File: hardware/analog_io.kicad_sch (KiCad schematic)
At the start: 32 parts, among them U1 TLV9162, U2 OPA1678

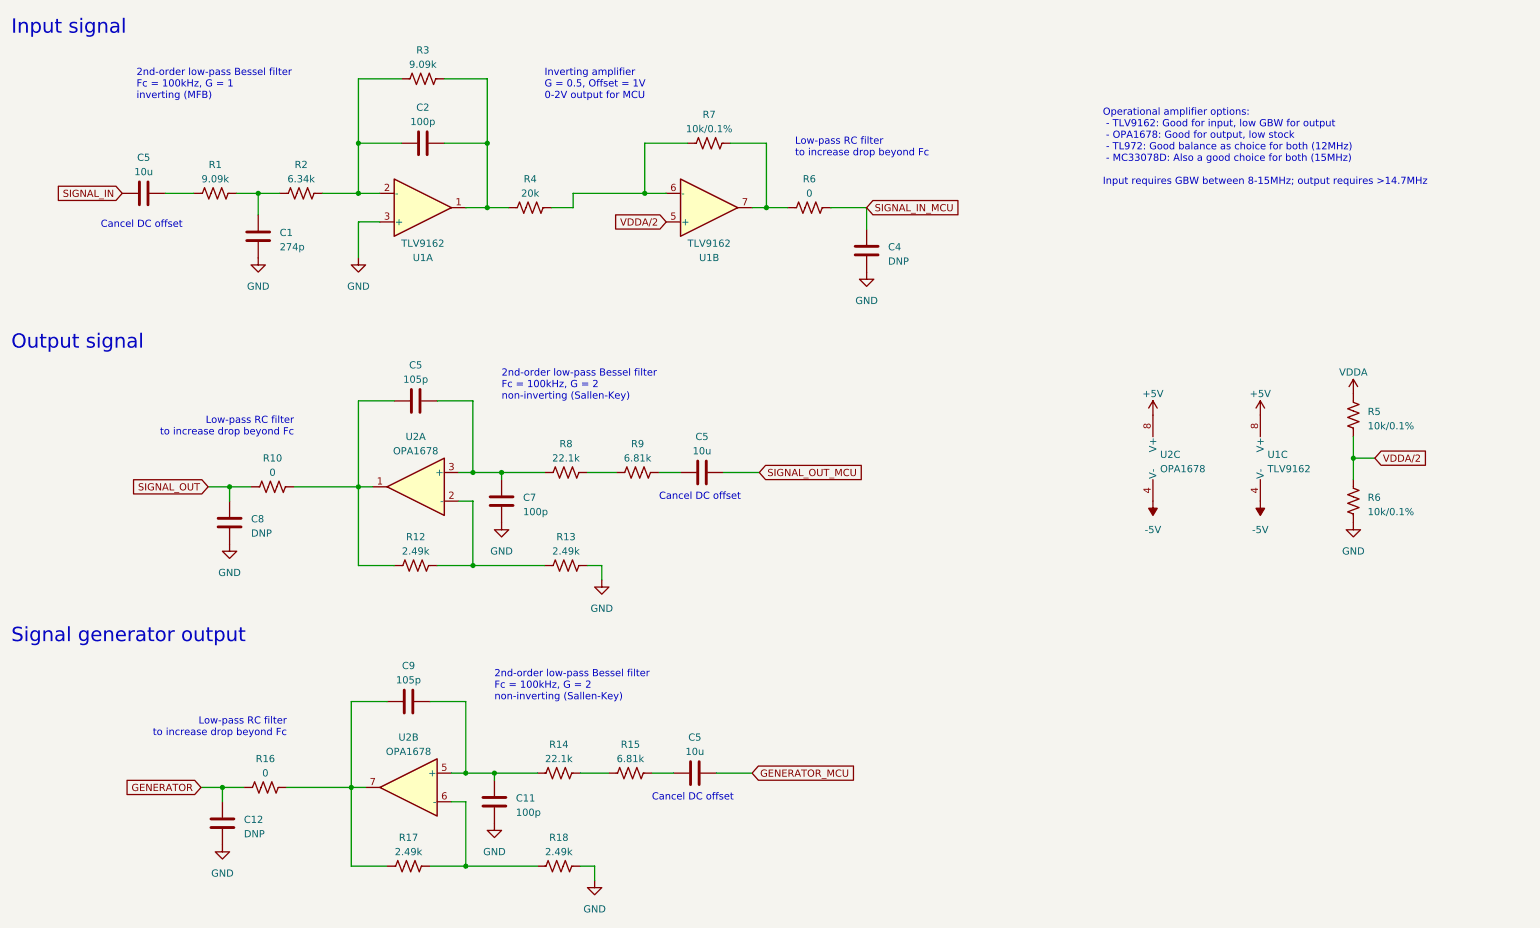
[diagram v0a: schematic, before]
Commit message: finalize pcb design; add layout file
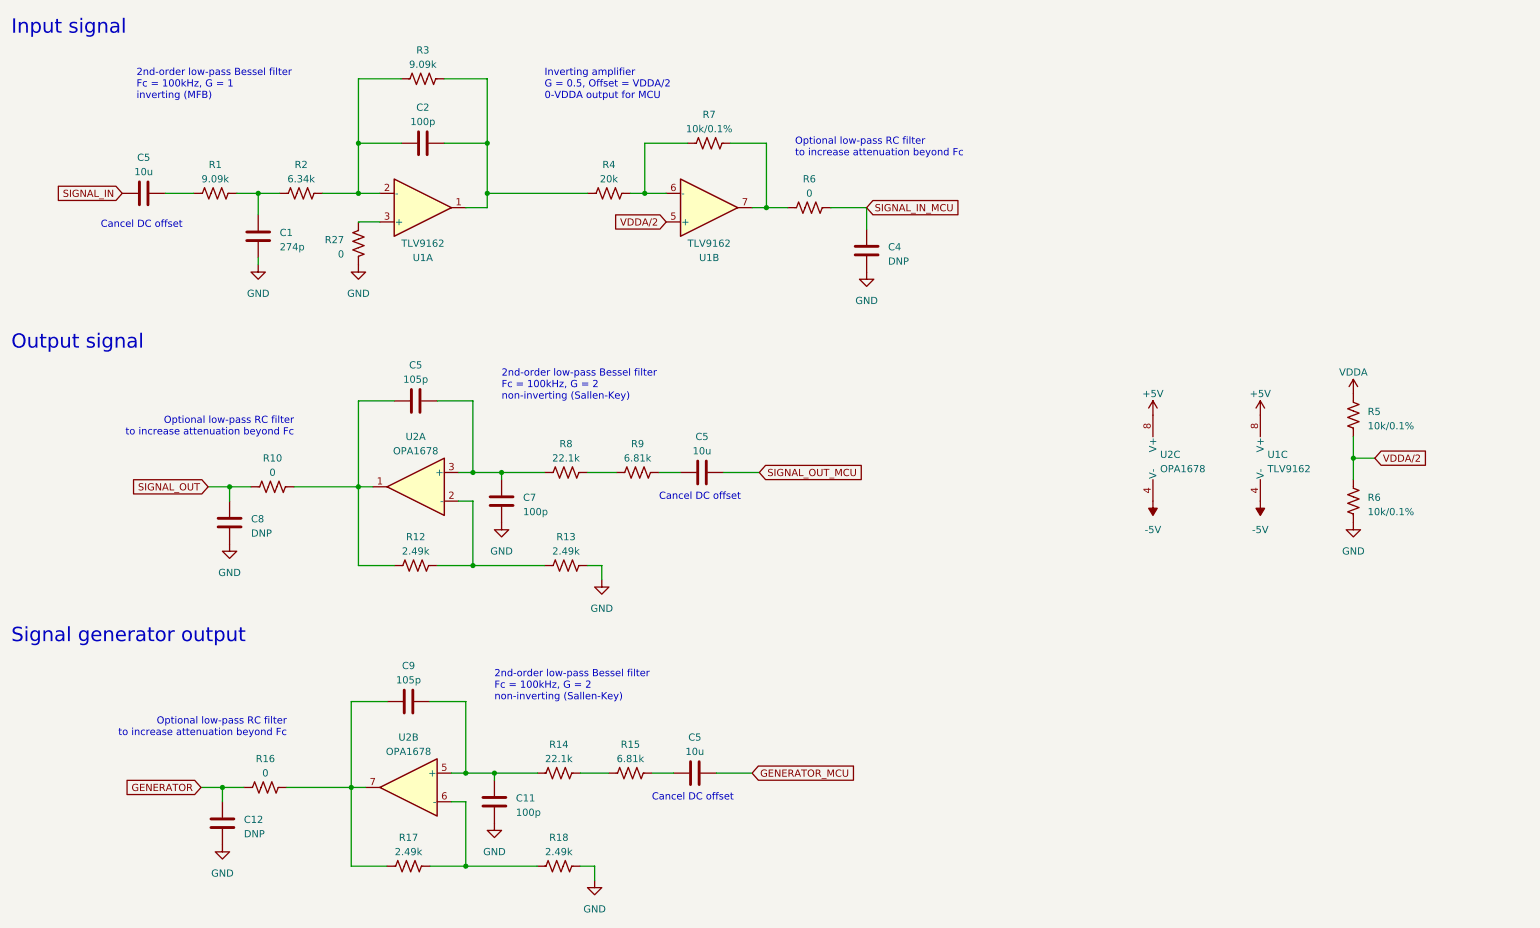
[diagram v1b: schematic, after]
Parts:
- added R27: 0, Resistor_SMD:R_0603_1608Metric, symbol Device:R_US
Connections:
- net GND: now also R27.1; no longer U1.3 (+)
- new net: R27.2, U1.3 (+)
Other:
- note added: "Inverting amplifier G = 0.5, Offset = VDDA/2 0-VDDA output for MCU"
- note added: "Optional low-pass RC filter to increase attenuation beyond Fc"
- note removed: "Inverting amplifier G = 0.5, Offset = 1V 0-2V output for MCU"
- note removed: "Low-pass RC filter to increase drop beyond Fc"
- note removed: "Operational amplifier options: - TLV9162: Good for input, low GBW for output - OPA1678: Good for output, low stock - TL972: Good balance as choice for both (12MHz) - MC33078D: Also a good choice for both (15MHz) Input requires GBW between 8-15MHz; output requires >14.7MHz"
- moved on the sheet: R4
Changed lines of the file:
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@@
   (title_block
     (title "Analog signal transformation")
-    (date "2023-08-08")
+    (date "2023-08-15")
     (company "bitgloo")
     (comment 1 "Released under the CERN Open Hardware Licence Version 2 - Strongly Reciprocal")
@@
   (junction (at 54.61 106.68) (diameter 0) (color 0 0 0 0)
   )
+  (junction (at 97.79 120.65) (diameter 0) (color 0 0 0 0)
+  )
+  (junction (at 101.6 157.48) (diameter 0) (color 0 0 0 0)
+  )
   (junction (at 128.27 54.61) (diameter 0) (color 0 0 0 0)
   )
-  (junction (at 97.79 120.65) (diameter 0) (color 0 0 0 0)
-  )
-  (junction (at 101.6 157.48) (diameter 0) (color 0 0 0 0)
-  )
-  (junction (at 100.33 57.15) (diameter 0) (color 0 0 0 0)
-  )
   (junction (at 77.47 54.61) (diameter 0) (color 0 0 0 0)
   )
   (junction (at 53.34 160.02) (diameter 0) (color 0 0 0 0)
   )
+  (junction (at 100.33 54.61) (diameter 0) (color 0 0 0 0)
+  )
   (junction (at 96.52 157.48) (diameter 0) (color 0 0 0 0)
   )
   (junction (at 59.69 54.61) (diameter 0) (color 0 0 0 0)
   )
-  (wire (pts (xy 128.27 54.61) (xy 115.57 54.61))
-    (stroke (width 0) (type default))
-  )
   (wire (pts (xy 57.15 160.02) (xy 53.34 160.02))
     (stroke (width 0) (type default))
@@
     (stroke (width 0) (type default))
   )
+  (wire (pts (xy 59.69 66.04) (xy 59.69 67.31))
+    (stroke (width 0) (type default))
+  )
   (wire (pts (xy 101.6 157.48) (xy 109.22 157.48))
     (stroke (width 0) (type default))
@@
     (stroke (width 0) (type default))
   )
-  (wire (pts (xy 115.57 54.61) (xy 115.57 57.15))
-    (stroke (width 0) (type default))
-  )
   (wire (pts (xy 97.79 120.65) (xy 110.49 120.65))
     (stroke (width 0) (type default))
@@
     (stroke (width 0) (type default))
   )
+  (wire (pts (xy 128.27 54.61) (xy 132.08 54.61))
+    (stroke (width 0) (type default))
+  )
   (wire (pts (xy 49.53 160.02) (xy 53.34 160.02))
     (stroke (width 0) (type default))
@@
     (stroke (width 0) (type default))
   )
-  (wire (pts (xy 100.33 45.72) (xy 100.33 57.15))
+  (wire (pts (xy 100.33 45.72) (xy 100.33 54.61))
     (stroke (width 0) (type default))
   )
@@
     (stroke (width 0) (type default))
   )
-  (wire (pts (xy 132.08 54.61) (xy 128.27 54.61))
+  (wire (pts (xy 125.73 54.61) (xy 128.27 54.61))
+    (stroke (width 0) (type default))
+  )
+  (wire (pts (xy 100.33 54.61) (xy 100.33 57.15))
     (stroke (width 0) (type default))
   )
@@
     (stroke (width 0) (type default))
   )
-  (wire (pts (xy 77.47 59.69) (xy 77.47 66.04))
-    (stroke (width 0) (type default))
-  )
   (wire (pts (xy 254 97.79) (xy 254 101.6))
     (stroke (width 0) (type default))
   )
-  (wire (pts (xy 111.76 57.15) (xy 115.57 57.15))
-    (stroke (width 0) (type default))
-  )
   (wire (pts (xy 118.11 104.14) (xy 123.19 104.14))
     (stroke (width 0) (type default))
@@
     (stroke (width 0) (type default))
   )
-  (wire (pts (xy 100.33 57.15) (xy 104.14 57.15))
-    (stroke (width 0) (type default))
-  )
   (wire (pts (xy 85.09 34.29) (xy 77.47 34.29))
     (stroke (width 0) (type default))
@@
   )
   (wire (pts (xy 71.12 54.61) (xy 77.47 54.61))
+    (stroke (width 0) (type default))
+  )
+  (wire (pts (xy 100.33 54.61) (xy 118.11 54.61))
     (stroke (width 0) (type default))
   )
@@
     (effects (font (size 1.27 1.27)) (justify left bottom))
   )
-  (text "Operational amplifier options:\n - TLV9162: Good for input, low GBW for output\n - OPA1678: Good for output, low stock\n - TL972: Good balance as choice for both (12MHz)\n - MC33078D: Also a good choice for both (15MHz)\n\nInput requires GBW between 8-15MHz; output requires >14.7MHz"
-    (at 209.55 53.34 0)
-    (effects (font (size 1.27 1.27)) (justify left bottom))
-  )
-  (text "Low-pass RC filter\nto increase drop beyond Fc" (at 154.94 48.26 0)
+  (text "Optional low-pass RC filter\nto increase attenuation beyond Fc"
+    (at 154.94 48.26 0)
     (effects (font (size 1.27 1.27)) (justify left bottom))
   )
@@
     (effects (font (size 1.27 1.27)) (justify left bottom))
   )
-  (text "Inverting amplifier\nG = 0.5, Offset = 1V\n0-2V output for MCU"
+  (text "Inverting amplifier\nG = 0.5, Offset = VDDA/2\n0-VDDA output for MCU"
     (at 110.49 38.1 0)
     (effects (font (size 1.27 1.27)) (justify left bottom))
@@
     (effects (font (size 1.27 1.27)) (justify left bottom))
   )
-  (text "Low-pass RC filter\nto increase drop beyond Fc" (at 66.04 97.79 0)
+  (text "Optional low-pass RC filter\nto increase attenuation beyond Fc"
+    (at 66.04 97.79 0)
     (effects (font (size 1.27 1.27)) (justify right bottom))
   )
@@
     (effects (font (size 2.54 2.54)) (justify left bottom))
   )
-  (text "Low-pass RC filter\nto increase drop beyond Fc" (at 64.77 151.13 0)
+  (text "Optional low-pass RC filter\nto increase attenuation beyond Fc"
+    (at 64.77 151.13 0)
     (effects (font (size 1.27 1.27)) (justify right bottom))
   )
@@
     )
   )
-  (symbol (lib_id "Device:R_US") (at 107.95 57.15 90) (unit 1)
-    (in_bom yes) (on_board yes) (dnp no) (fields_autoplaced)
-    (property "Reference" "R4" (at 107.95 52.07 90)
-      (effects (font (size 1.27 1.27)))
-    )
-    (property "Value" "20k" (at 107.95 54.61 90)
-      (effects (font (size 1.27 1.27)))
-    )
-    (property "Footprint" "Resistor_SMD:R_0603_1608Metric" (at 108.204 56.134 90)
-      (effects (font (size 1.27 1.27)) hide)
-    )
-    (property "Datasheet" "~" (at 107.95 57.15 0)
-      (effects (font (size 1.27 1.27)) hide)
-    )
-    (property "Part Number" "RT0603DRE0720KL" (at 107.95 57.15 0)
+  (symbol (lib_id "Device:R_US") (at 121.92 54.61 90) (unit 1)
+    (in_bom yes) (on_board yes) (dnp no) (fields_autoplaced)
+    (property "Reference" "R4" (at 121.92 49.53 90)
+      (effects (font (size 1.27 1.27)))
+    )
+    (property "Value" "20k" (at 121.92 52.07 90)
+      (effects (font (size 1.27 1.27)))
+    )
+    (property "Footprint" "Resistor_SMD:R_0603_1608Metric" (at 122.174 53.594 90)
+      (effects (font (size 1.27 1.27)) hide)
+    )
+    (property "Datasheet" "~" (at 121.92 54.61 0)
+      (effects (font (size 1.27 1.27)) hide)
+    )
+    (property "Part Number" "RT0603DRE0720KL" (at 121.92 54.61 0)
       (effects (font (size 1.27 1.27)) hide)
     )
@@
     )
   )
-  (symbol (lib_id "power:GND") (at 59.69 66.04 0) (unit 1)
-    (in_bom yes) (on_board yes) (dnp no) (fields_autoplaced)
-    (property "Reference" "#PWR01" (at 59.69 72.39 0)
-      (effects (font (size 1.27 1.27)) hide)
-    )
-    (property "Value" "GND" (at 59.69 71.12 0)
-      (effects (font (size 1.27 1.27)))
-    )
-    (property "Footprint" "" (at 59.69 66.04 0)
-      (effects (font (size 1.27 1.27)) hide)
-    )
-    (property "Datasheet" "" (at 59.69 66.04 0)
+  (symbol (lib_id "power:GND") (at 59.69 67.31 0) (unit 1)
+    (in_bom yes) (on_board yes) (dnp no) (fields_autoplaced)
+    (property "Reference" "#PWR01" (at 59.69 73.66 0)
+      (effects (font (size 1.27 1.27)) hide)
+    )
+    (property "Value" "GND" (at 59.69 72.39 0)
+      (effects (font (size 1.27 1.27)))
+    )
+    (property "Footprint" "" (at 59.69 67.31 0)
+      (effects (font (size 1.27 1.27)) hide)
+    )
+    (property "Datasheet" "" (at 59.69 67.31 0)
       (effects (font (size 1.27 1.27)) hide)
     )
@@
         (path "/c291319b-d76e-4fda-91cc-061acff65f9f/684072e7-f538-4528-bfb8-b14c31b5b1f0"
           (reference "R12") (unit 1)
+        )
+      )
+    )
+  )
+  (symbol (lib_id "Device:R_US") (at 77.47 63.5 0) (mirror x) (unit 1)
+    (in_bom yes) (on_board yes) (dnp no)
+    (property "Reference" "R27" (at 74.93 62.865 0)
+      (effects (font (size 1.27 1.27)) (justify right))
+    )
+    (property "Value" "0" (at 74.93 65.405 0)
+      (effects (font (size 1.27 1.27)) (justify right))
+    )
+    (property "Footprint" "Resistor_SMD:R_0603_1608Metric" (at 78.486 63.246 90)
+      (effects (font (size 1.27 1.27)) hide)
+    )
+    (property "Datasheet" "~" (at 77.47 63.5 0)
+      (effects (font (size 1.27 1.27)) hide)
+    )
+    (property "Part Number" "RMCF0603ZT0R00" (at 77.47 63.5 0)
+      (effects (font (size 1.27 1.27)) hide)
+    )
+    (pin "1")
+    (pin "2")
+    (instances
+      (project "DSP PAW add-on board"
+        (path "/c291319b-d76e-4fda-91cc-061acff65f9f/684072e7-f538-4528-bfb8-b14c31b5b1f0"
+          (reference "R27") (unit 1)
         )
       )
@@
     )
   )
-  (symbol (lib_id "power:GND") (at 77.47 66.04 0) (unit 1)
-    (in_bom yes) (on_board yes) (dnp no) (fields_autoplaced)
-    (property "Reference" "#PWR02" (at 77.47 72.39 0)
-      (effects (font (size 1.27 1.27)) hide)
-    )
-    (property "Value" "GND" (at 77.47 71.12 0)
-      (effects (font (size 1.27 1.27)))
-    )
-    (property "Footprint" "" (at 77.47 66.04 0)
-      (effects (font (size 1.27 1.27)) hide)
-    )
-    (property "Datasheet" "" (at 77.47 66.04 0)
-      (effects (font (size 1.27 1.27)) hide)
-    )
+  (symbol (lib_id "power:GND") (at 77.47 67.31 0) (unit 1)
+    (in_bom yes) (on_board yes) (dnp no) (fields_autoplaced)
+    (property "Reference" "#PWR02" (at 77.47 73.66 0)
+      (effects (font (size 1.27 1.27)) hide)
+    )
+    (property "Value" "GND" (at 77.47 72.39 0)
+      (effects (font (size 1.27 1.27)))
+    )
+    (property "Footprint" "" (at 77.47 67.31 0)
+      (effects (font (size 1.27 1.27)) hide)
+    )
+    (property "Datasheet" "" (at 77.47 67.31 0)
+      (effects (font (size 1.27 1.27)) hide)
+    )

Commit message: pcb design finalization
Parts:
- C1: LCSC Part # (none) -> C107084
- C11, C2, C5, C7, C9: LCSC Part # (none) -> C160903
- C12, C4, C8: DNP (none) -> T
- C5: LCSC Part # (none) -> C15850
- R1, R3: value 9.09k -> 9.09k/0.1%; LCSC Part # (none) -> C861611
- R10, R16, R27, R6: LCSC Part # (none) -> C21189
- R12, R13, R17, R18: value 2.49k -> 2.49k/0.1%; LCSC Part # (none) -> C861299
- R14, R8: value 22.1k -> 22.1k/0.1%; LCSC Part # (none) -> C861759
- R15, R9: value 6.81k -> 6.81k/0.1%; LCSC Part # (none) -> C326739
- R2: value 6.34k -> 6.34k/0.1%; LCSC Part # (none) -> C861532
- R4: value 20k -> 20k/0.1%; LCSC Part # (none) -> C5123584
- R5, R6, R7: LCSC Part # (none) -> C319939
- U1: LCSC Part # (none) -> C54272
- U2: LCSC Part # (none) -> C192421
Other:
- note added: "Can substitute LM833"
- title: Analog signal transformation -> DSP PAW add-on board
